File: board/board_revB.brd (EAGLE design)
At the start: 94 x 44.5 mm, 74 parts, among them Q1 ULN2003AS, Q2 ULN2003AD, Y1 8Mhz

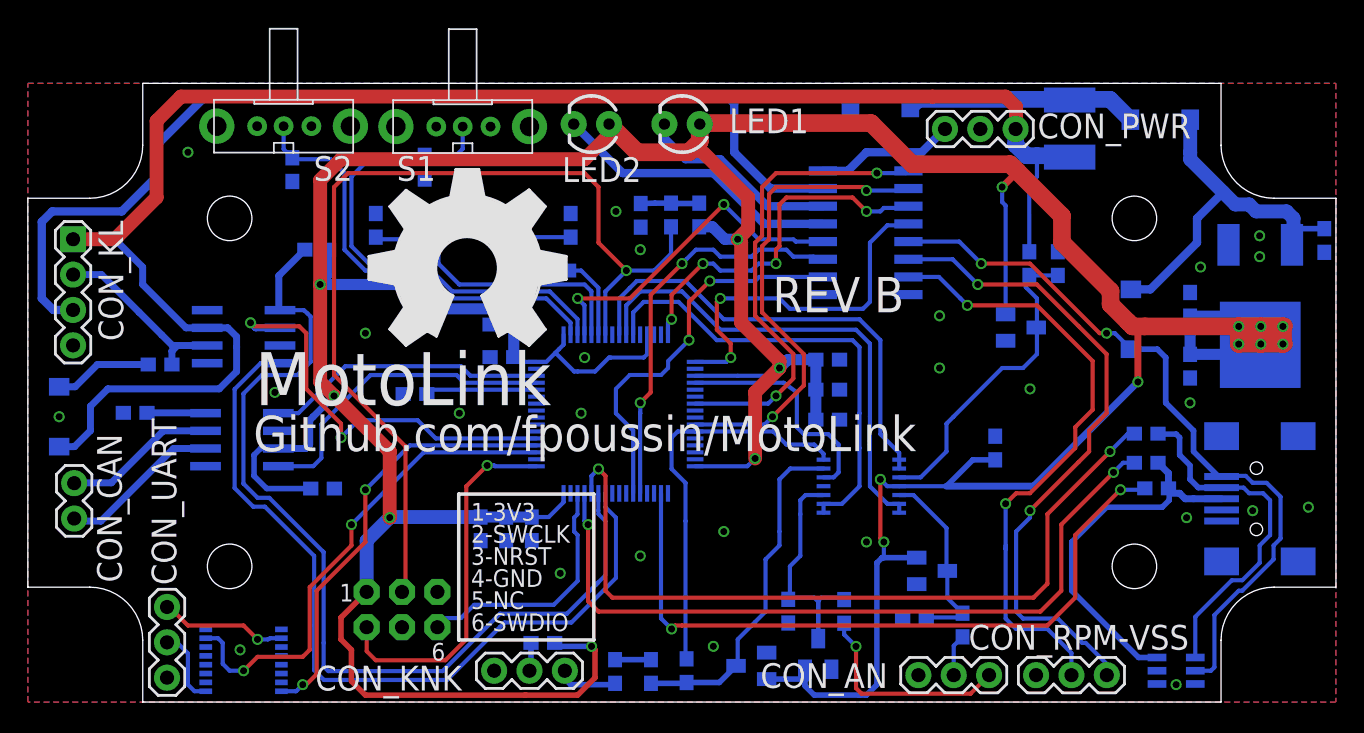
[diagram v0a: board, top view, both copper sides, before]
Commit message: [Board Rev B] Multiple improvements. Adding extra UART.
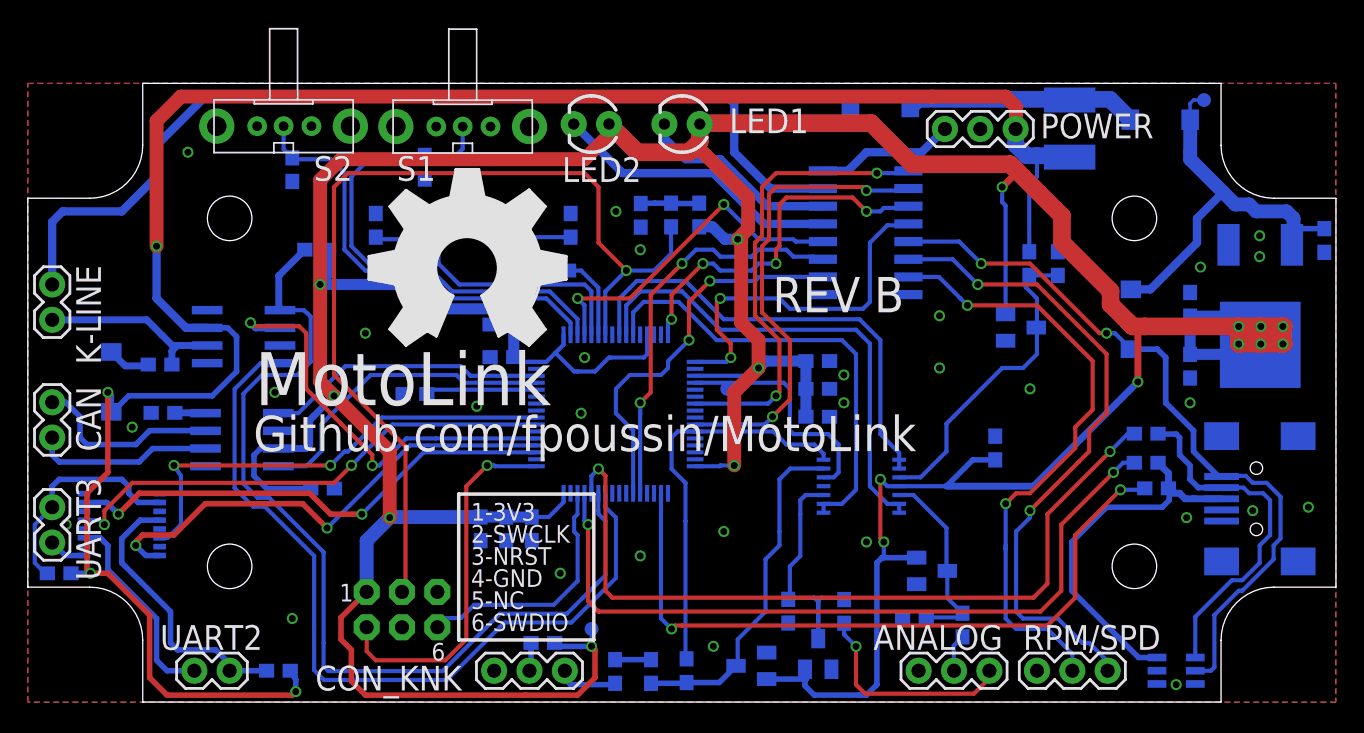
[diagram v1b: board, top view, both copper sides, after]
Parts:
- removed CON_KL: (no value), SparkFun-Connectors:1X04
- added CON_K-LINE, CON_UART1: M02PTH, SparkFun-Connectors:1X02
- added R18, R9: 4.7K, SparkFun-Resistors:0603-RES
- added TP1, TP2, TP3: (no value), microbuilder:TESTPOINT_ROUND_1MM
- CON_UART: value (none) -> M02PTH; device SparkFun-Connectors:1X03 -> SparkFun-Connectors:1X02
- moved CON_UART 14.8 mm to (1.75, 14.0), turned to 270 degrees
- moved Q1 13.1 mm to (6.75, 12.8)
- moved CON_CAN 6.03 mm to (1.75, 19.0)
- moved D6 4.51 mm to (6.00, 23.0)
- moved R3 2.00 mm to (9.71, 20.8)
- moved C24 0.75 mm to (56.8, 20.5)
- moved C26 0.72 mm to (56.8, 24.5)
- moved C25 0.72 mm to (56.8, 22.5)
- moved CON_RPM-VSS 0.32 mm to (72.5, 2.25)
- moved CON_AN 0.32 mm to (64.0, 2.25)
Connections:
- net UART_RXD_OUT renamed UART3_RXD_OUT
- removed net UART_TXD_OUT: CON_UART.3, Q1.10
- new net UART2_RXD_OUT: CON_UART1.2, Q1.3
- new net UART2_TXD_OUT: CON_UART1.1, Q1.12, R9.1
- new net UART3_TXD_OUT: CON_UART.1, Q1.10, R18.1
- new net USART2_RX: Q1.14, STM32.56
- new net USART2_TX: Q1.5, STM32.55
- net +12V: now also R18.2, R9.2; no longer CON_KL.1
- net +3V3: now also TP2.P$1
- net DAC1: now also TP1.P$1
- net GND: no longer CON_KL.4, CON_UART.1
- net K-LINE: now also CON_K-LINE.2; no longer CON_KL.2
- net SCS: now also CON_K-LINE.1; no longer CON_KL.3
- net VCC: now also TP3.P$1
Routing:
- net USART2_TX: track 0.00 -> 36.2 mm, vias 0 -> 2
- net USART2_RX: track 0.00 -> 33.8 mm, vias 0 -> 2
- net +12V: track 123.7 -> 149.0 mm, vias 0 -> 4
- net UART2_TXD_OUT: track 0.00 -> 20.2 mm
- net UART3_TXD_OUT: track 0.00 -> 16.1 mm
- net UART2_RXD_OUT: track 0.00 -> 14.7 mm
- net UART_TXD_OUT: track 9.20 -> 0.00 mm, vias 1 -> 0
- net SCS: track 74.0 -> 69.7 mm
- net USART3_RX: track 31.3 -> 35.4 mm
- net N$13: track 7.06 -> 3.11 mm
- net UART3_RXD_OUT: track 5.56 -> 2.67 mm
- net CANH: track 11.0 -> 13.6 mm
- net VCC: track 26.8 -> 29.1 mm
- net N$8: track 4.22 -> 2.22 mm
- net +3V3: track 347.1 -> 345.4 mm
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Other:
- board text added: "ANALOG"
- board text added: "CAN"
- board text added: "DEBUG"
- board text added: "K-LINE"
- board text added: "POWER"
- board text added: "RPM/SPD"
- board text added: "UART2"
- board text added: "UART3"

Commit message: [Board Rev B] Updating various components.
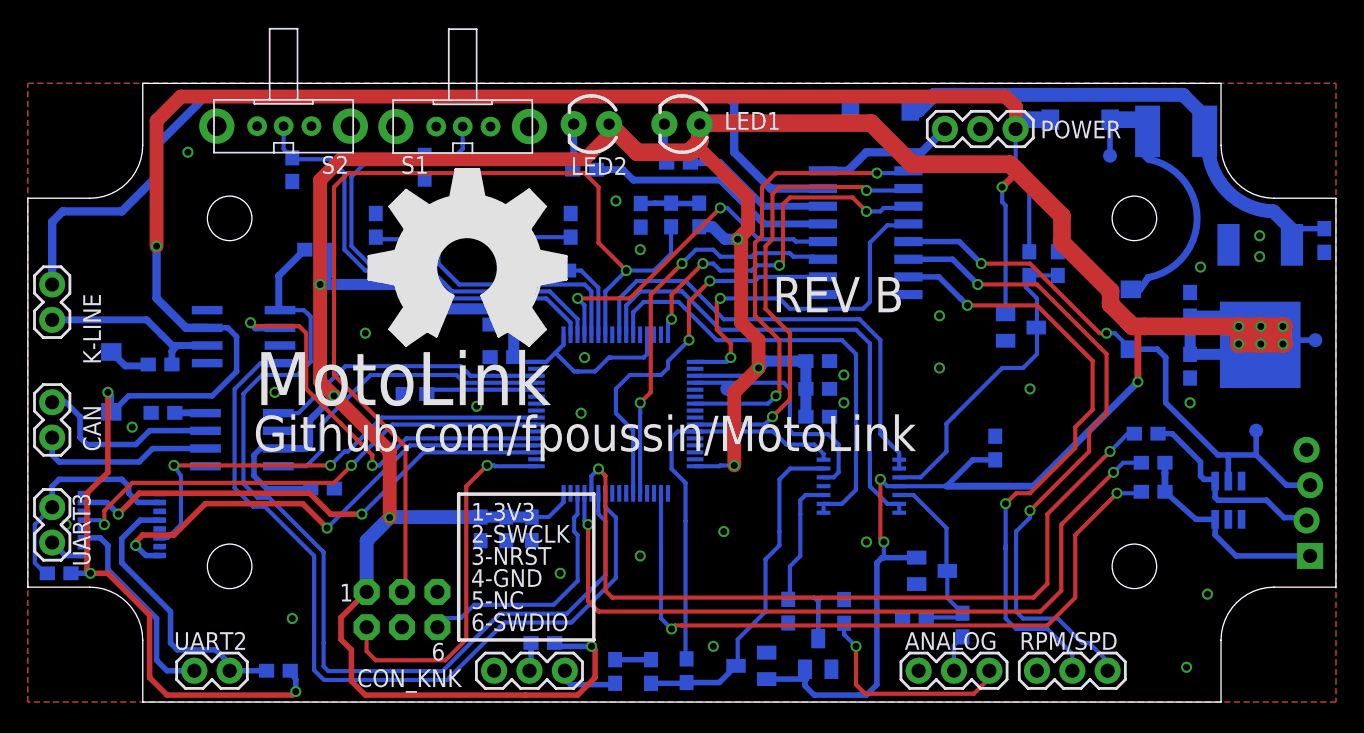
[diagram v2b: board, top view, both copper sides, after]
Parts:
- removed CON_UART: M02PTH, SparkFun-Connectors:1X02
- removed CON_USB: USBSMD, SparkFun-Connectors:USB-MINIB
- added CON_UART2: M02PTH, SparkFun-Connectors:1X02
- added JP1: (no value), SparkFun-Connectors:1X04_LOCK
- added R21, R22: 56R, SparkFun-Resistors:0603-RES
- added TP4: (no value), microbuilder:TESTPOINT_ROUND_1MM
- R30, R5: value 10K -> 100K
- R31: value 1K -> 10K
- R32, R4, R6, R7: value 10K -> 1M
- R8: value 47K -> 470K
- moved TP2 56.0 mm to (92.5, 26.0), turned to 90 degrees
- moved CON_UART1 17.3 mm to (1.75, 14.0), turned to 270 degrees
- moved TVS2 12.8 mm to (86.2, 14.5), turned to 0 degrees
- moved TP3 7.85 mm to (77.8, 39.2)
- moved F1 7.65 mm to (82.5, 41.0), turned to 0 degrees
- moved D1 5.75 mm to (75.6, 41.8)
- moved R15 0.50 mm to (80.8, 17.2)
- moved R17 0.35 mm to (80.8, 15.1)
- moved TVS1 0.25 mm to (61.2, 42.5)
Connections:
- removed net N$9: D1.A, F1.1, TVS1.C
- new net N$15: Q2.14, R22.2
- new net N$19: LED1.K, R22.1
- new net N$20: C1.1, F1.1, IC_REG.3, TVS1.C
- net +12V: now also D1.A; no longer F1.2
- net GND: now also JP1.4; no longer CON_USB.GND
- net N$10: now also LED2.K, R21.1; no longer LED1.K, Q2.14
- net N$11: now also R21.2; no longer LED2.K
- net N$17: now also JP1.2; no longer CON_USB.D-
- net N$7: now also JP1.1; no longer CON_USB.D+
- net UART2_RXD_OUT: now also CON_UART2.2; no longer CON_UART1.2
- net UART2_TXD_OUT: now also CON_UART2.1; no longer CON_UART1.1
- net UART3_RXD_OUT: now also CON_UART1.2; no longer CON_UART.2
- net UART3_TXD_OUT: now also CON_UART1.1; no longer CON_UART.1
- net USB_VBUS: now also JP1.3, TP4.P$1; no longer CON_USB.VBUS
- net VCC: now also F1.2; no longer C1.1, IC_REG.3
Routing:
- net N$20: track 0.00 -> 36.3 mm
- net N$9: track 16.7 -> 0.00 mm
- net N$7: track 27.1 -> 15.0 mm
- net USB_VBUS: track 53.0 -> 41.6 mm
- net N$10: track 14.4 -> 3.29 mm
- net N$15: track 0.00 -> 10.8 mm
- net N$17: track 25.3 -> 14.5 mm
- net VCC: track 29.1 -> 20.2 mm
- net N$11: track 20.9 -> 17.9 mm
- net N$19: track 0.00 -> 2.84 mm
- net +3V3: track 345.4 -> 346.6 mm
- net +12V: track 149.0 -> 148.3 mm
- net USB_DP: track 54.6 -> 55.1 mm

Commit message: [Board Rev B] USB connector renamed.
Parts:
- renumbered JP1 to CON_USB
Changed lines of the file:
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@@
 <attribute name="VALUE" x="38.984" y="39.393" size="0.4064" layer="28" font="vector" rot="MR180"/>
 </element>
-<element name="JP1" library="SparkFun-Connectors" package="1X04_LOCK" value="" x="92" y="10.5" rot="MR90"/>
+<element name="CON_USB" library="SparkFun-Connectors" package="1X04_LOCK" value="" x="92" y="10.5" smashed="yes" rot="MR90">
+<attribute name="NAME" x="89.0788" y="10.4038" size="1.27" layer="26" font="vector" ratio="16" rot="MR90"/>
+<attribute name="VALUE" x="88.825" y="9.23" size="1.27" layer="28" rot="MR90"/>
+</element>
 <element name="TP2" library="microbuilder" package="TESTPOINT_ROUND_1MM" value="" x="92.5" y="26" smashed="yes" rot="MR90">
 <attribute name="NAME" x="93.377" y="25.357" size="1.27" layer="26" font="vector" ratio="16" rot="MR270"/>
@@
 <via x="58.625" y="23.5" extent="1-16" drill="0.5"/>
 <via x="58.625" y="21.5" extent="1-16" drill="0.5"/>
-<contactref element="JP1" pad="4"/>
+<contactref element="CON_USB" pad="4"/>
 </signal>
 <signal name="+3V3">
@@
 <wire x1="81.75" y1="24.75" x2="81.75" y2="21.5" width="0.4064" layer="16"/>
 <wire x1="77.5" y1="26.5" x2="78.1" y2="26.5" width="0.3" layer="16"/>
-<contactref element="JP1" pad="3"/>
+<contactref element="CON_USB" pad="3"/>
 <wire x1="92.127" y1="15.58" x2="90.42" y2="15.58" width="0.4" layer="16"/>
 <wire x1="90.42" y1="15.58" x2="88.25" y2="17.75" width="0.4" layer="16"/>
@@
 <contactref element="R16" pad="1"/>
 <contactref element="TVS2" pad="4"/>
-<contactref element="JP1" pad="2"/>
+<contactref element="CON_USB" pad="2"/>
 <wire x1="81.1975" y1="19.28" x2="82.22" y2="19.28" width="0.4" layer="16"/>
 <wire x1="82.22" y1="19.28" x2="84.25" y2="17.25" width="0.4" layer="16"/>
@@
 <wire x1="81.6975" y1="16.4425" x2="81.6975" y2="17.1925" width="0.5" layer="16"/>
 <contactref element="TVS2" pad="3"/>
-<contactref element="JP1" pad="1"/>
+<contactref element="CON_USB" pad="1"/>
 <wire x1="92.127" y1="10.5" x2="86.8025" y2="10.5" width="0.4" layer="16"/>
 <wire x1="85.3" y1="13.1249" x2="85.3" y2="12.0025" width="0.4" layer="16"/>

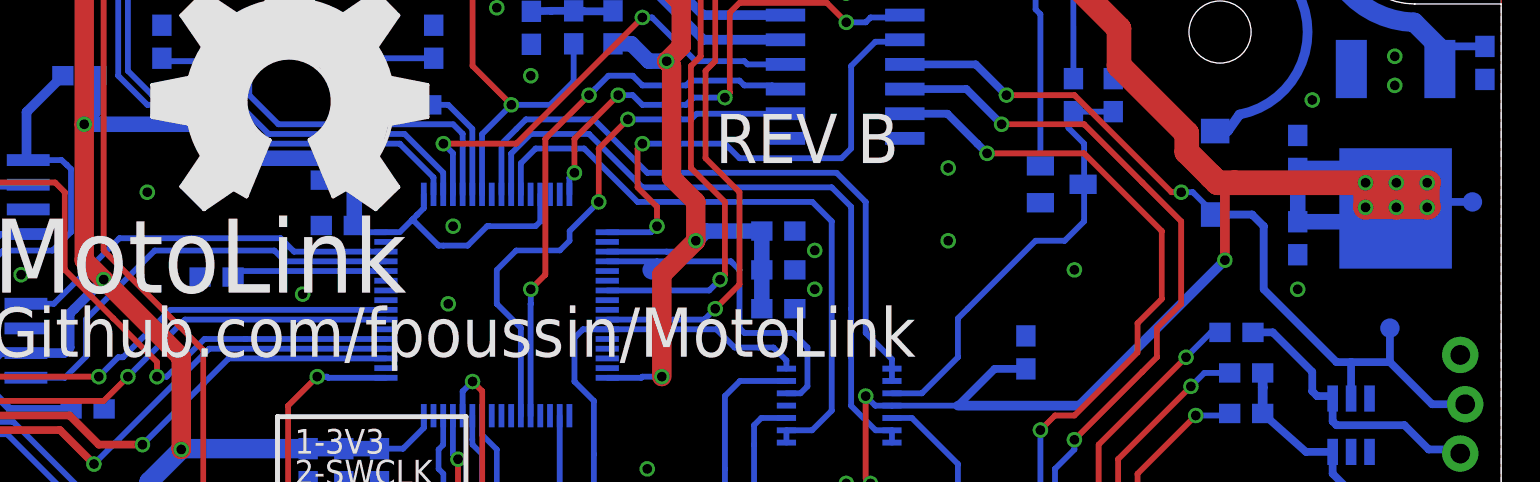
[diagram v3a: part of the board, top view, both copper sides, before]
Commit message: [Board Rev B] Adding voltage reference for VDDA.
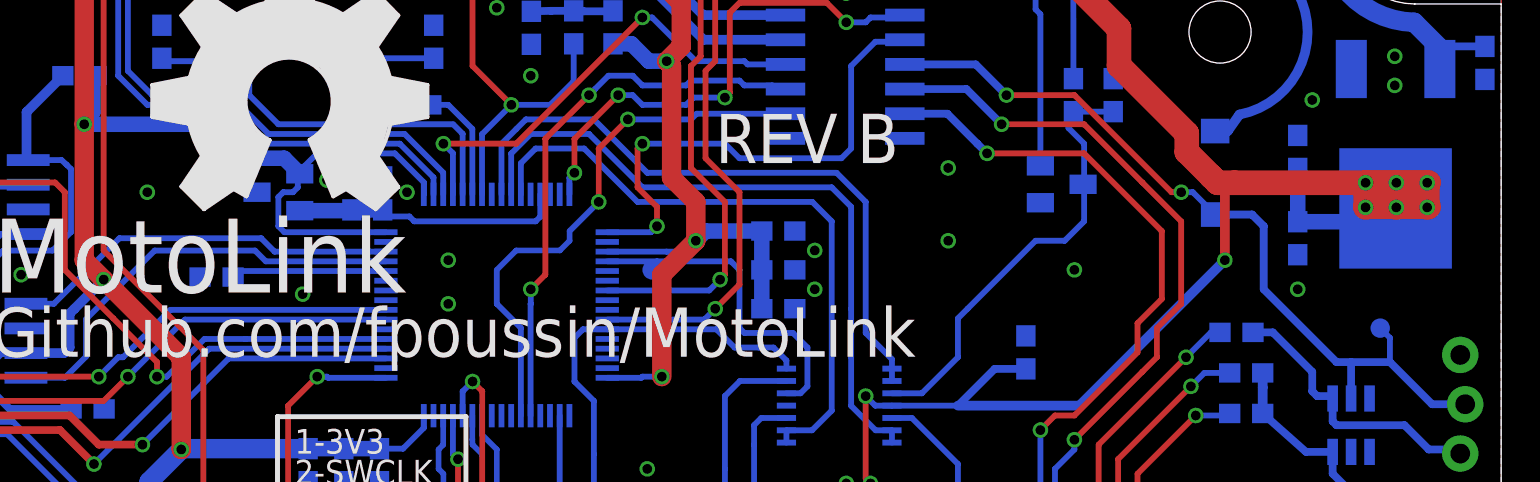
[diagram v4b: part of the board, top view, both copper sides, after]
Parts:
- removed TP2: (no value), microbuilder:TESTPOINT_ROUND_1MM
- added IC_REF: MC1525TT, microchip:SOT23
- moved C30 2.41 mm to (36.4, 26.4), turned to 90 degrees
- moved C31 1.81 mm to (34.8, 26.4), turned to 90 degrees
- moved TP4 0.50 mm to (87.8, 19.5)
- renumbered IC_REG to IC_REG1
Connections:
- new net VAN: C30.1, C31.1, IC_REF.2, STM32.13
- net +3V3: now also IC_REF.1; no longer C30.1, C31.1, STM32.13, TP2.P$1
- net GND: now also IC_REF.3
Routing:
- net VAN: track 0.00 -> 13.9 mm
- net +3V3: track 346.6 -> 339.1 mm
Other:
- board text added: "2.5V"
- board text added: "3.3V"

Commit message: [Board] Fix files
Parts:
- removed IC_REF: MC1525TT, microchip:SOT23
- added IC_EE: 25LC040ST, microchip:TSSOP8
- added TP2: (no value), microbuilder:TESTPOINT_ROUND_1MM
- moved C30 2.41 mm to (34.1, 27.1), turned to 0 degrees
- moved C31 1.81 mm to (34.1, 24.8), turned to 0 degrees
- moved TP4 0.50 mm to (88.2, 19.5)
- renumbered IC_REG1 to IC_REG
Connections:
- removed net VAN: C30.1, C31.1, IC_REF.2, STM32.13
- new net SPI2_MISO: IC_EE.2, STM32.35
- new net SPI2_MOSI: IC_EE.5, STM32.36
- new net SPI2_NSS: IC_EE.1, STM32.33
- new net SPI2_SCK: IC_EE.6, STM32.34
- net +3V3: now also C30.1, C31.1, IC_EE.3, IC_EE.8, STM32.13, TP2.P$1; no longer IC_REF.1
- net GND: now also IC_EE.4; no longer IC_REF.3
- net USB_CTRL: now also STM32.39; no longer STM32.34
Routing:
- net +3V3: track 339.1 -> 359.9 mm, vias 17 -> 19
- net VAN: track 13.9 -> 0.00 mm
- net SPI2_MISO: track 0.00 -> 11.4 mm
- net SPI2_MOSI: track 0.00 -> 6.07 mm
- net AN_KNOCK: track 28.5 -> 34.6 mm, vias 0 -> 2
- net SPI2_NSS: track 0.00 -> 5.66 mm
- net SPI2_SCK: track 0.00 -> 5.36 mm
- net USB_CTRL: track 51.2 -> 52.2 mm
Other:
- board text removed: "2.5V"
- board text removed: "3.3V"
